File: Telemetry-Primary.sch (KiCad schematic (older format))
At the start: 34 parts

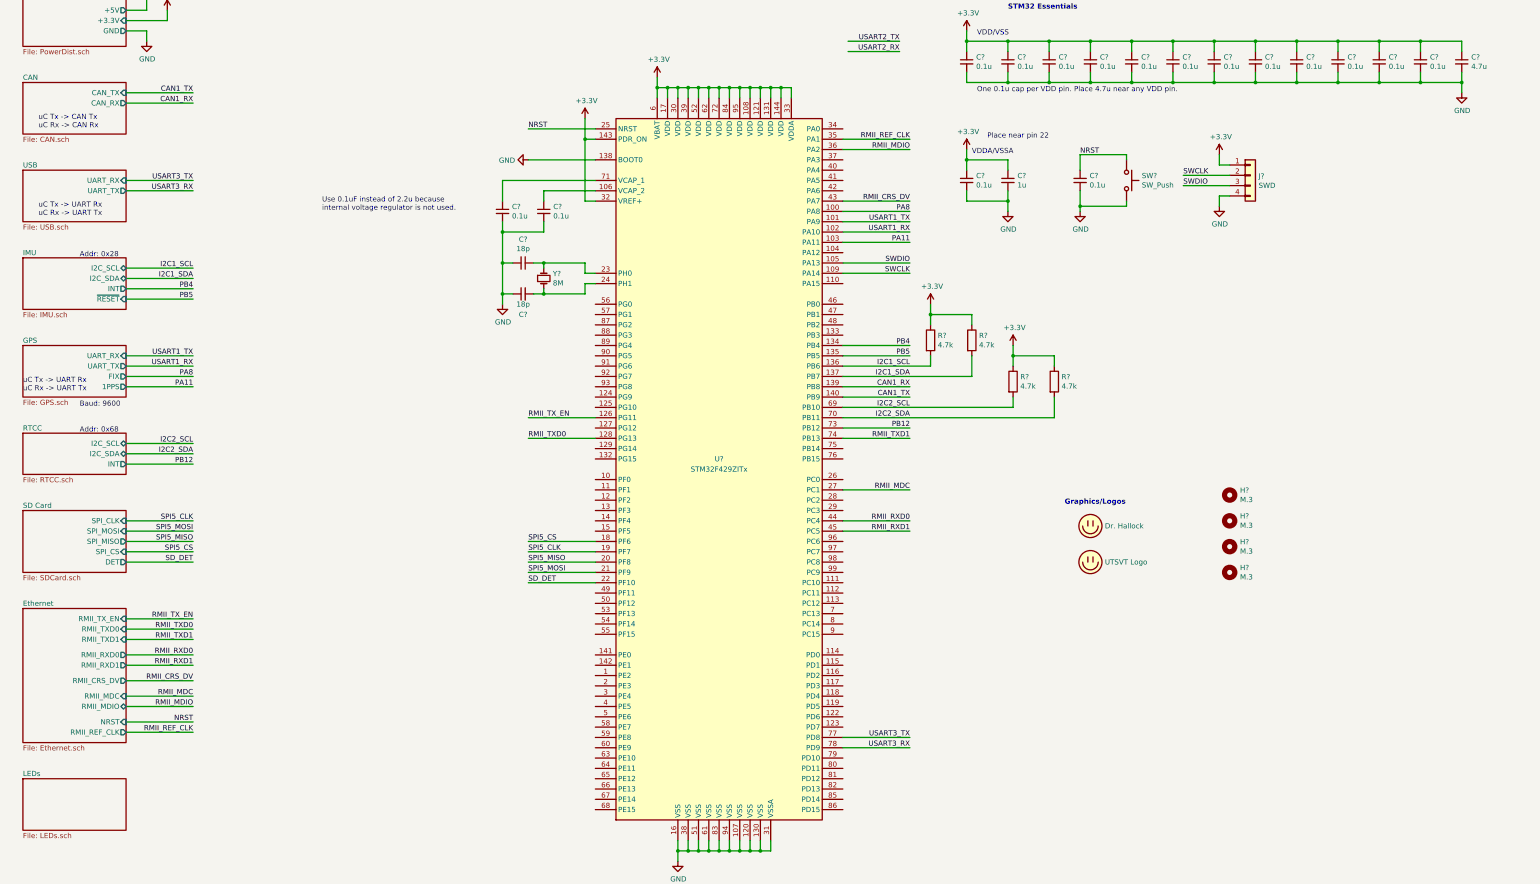
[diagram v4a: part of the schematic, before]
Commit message: Adds logic analyzer points and LEDs
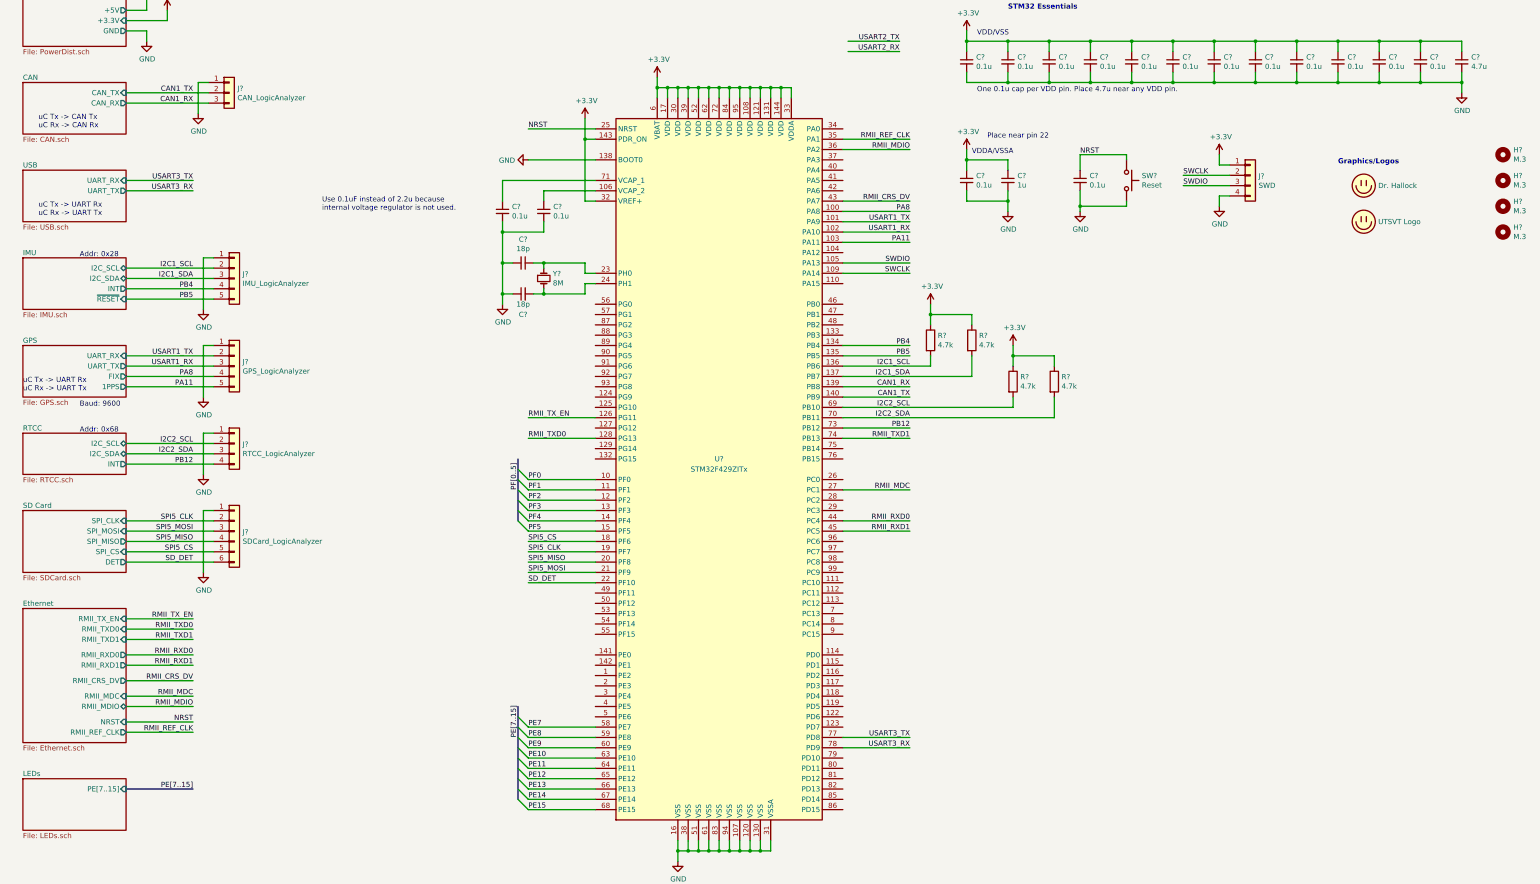
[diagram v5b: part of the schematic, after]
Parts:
- added J?: IMU_LogicAnalyzer, Connector_PinHeader_2.54mm:PinHeader_1x05_P2.54mm_Vertical, symbol Connector_Generic:Conn_01x05
- added J?: GPS_LogicAnalyzer, Connector_PinHeader_2.54mm:PinHeader_1x05_P2.54mm_Vertical, symbol Connector_Generic:Conn_01x05
- added J?: RTCC_LogicAnalyzer, Connector_PinHeader_2.54mm:PinHeader_1x04_P2.54mm_Vertical, symbol Connector_Generic:Conn_01x04
- added J?: SDCard_LogicAnalyzer, symbol Connector_Generic:Conn_01x06
- added J?: CAN_LogicAnalyzer, symbol Connector_Generic:Conn_01x03
- SW?: value SW_Push -> Reset; footprint (none) -> Button_Switch_SMD:SW_SPST_B3SL-1002P; P/N (none) -> EVQ-7Q203W or B3SL-1002P
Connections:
- net CAN1_RX: now also J?.3 (Pin_3)
- net CAN1_TX: now also J?.2 (Pin_2)
- net GND: now also J?.1 (Pin_1), J?.1 (Pin_1), J?.1 (Pin_1), J?.1 (Pin_1), J?.1 (Pin_1)
- net I2C1_SCL: now also J?.2 (Pin_2)
- net I2C1_SDA: now also J?.3 (Pin_3)
- net I2C2_SCL: now also J?.2 (Pin_2)
- net I2C2_SDA: now also J?.3 (Pin_3)
- net PA11: now also J?.5 (Pin_5)
- net PA8: now also J?.4 (Pin_4)
- net PB12: now also J?.4 (Pin_4)
- net PB4: now also J?.4 (Pin_4)
- net PB5: now also J?.5 (Pin_5)
- net SD_DET: now also J?.6 (Pin_6)
- net SPI5_CLK: now also J?.2 (Pin_2)
- net SPI5_CS: now also J?.5 (Pin_5)
- net SPI5_MISO: now also J?.4 (Pin_4)
- net SPI5_MOSI: now also J?.3 (Pin_3)
- net USART1_RX: now also J?.3 (Pin_3)
- net USART1_TX: now also J?.2 (Pin_2)
- net PF0: now reaches U?.10 (PF0)
- net PF1: now reaches U?.11 (PF1)
- net PF2: now reaches U?.12 (PF2)
- net PF3: now reaches U?.13 (PF3)
- net PF4: now reaches U?.14 (PF4)
- net PF5: now reaches U?.15 (PF5)
- net PE7: now reaches U?.58 (PE7)
- net PE8: now reaches U?.59 (PE8)
- net PE9: now reaches U?.60 (PE9)
- net PE10: now reaches U?.63 (PE10)
- net PE11: now reaches U?.64 (PE11)
- net PE12: now reaches U?.65 (PE12)
- net PE13: now reaches U?.66 (PE13)
- net PE14: now reaches U?.67 (PE14)
- net PE15: now reaches U?.68 (PE15)
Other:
- moved on the sheet: H?

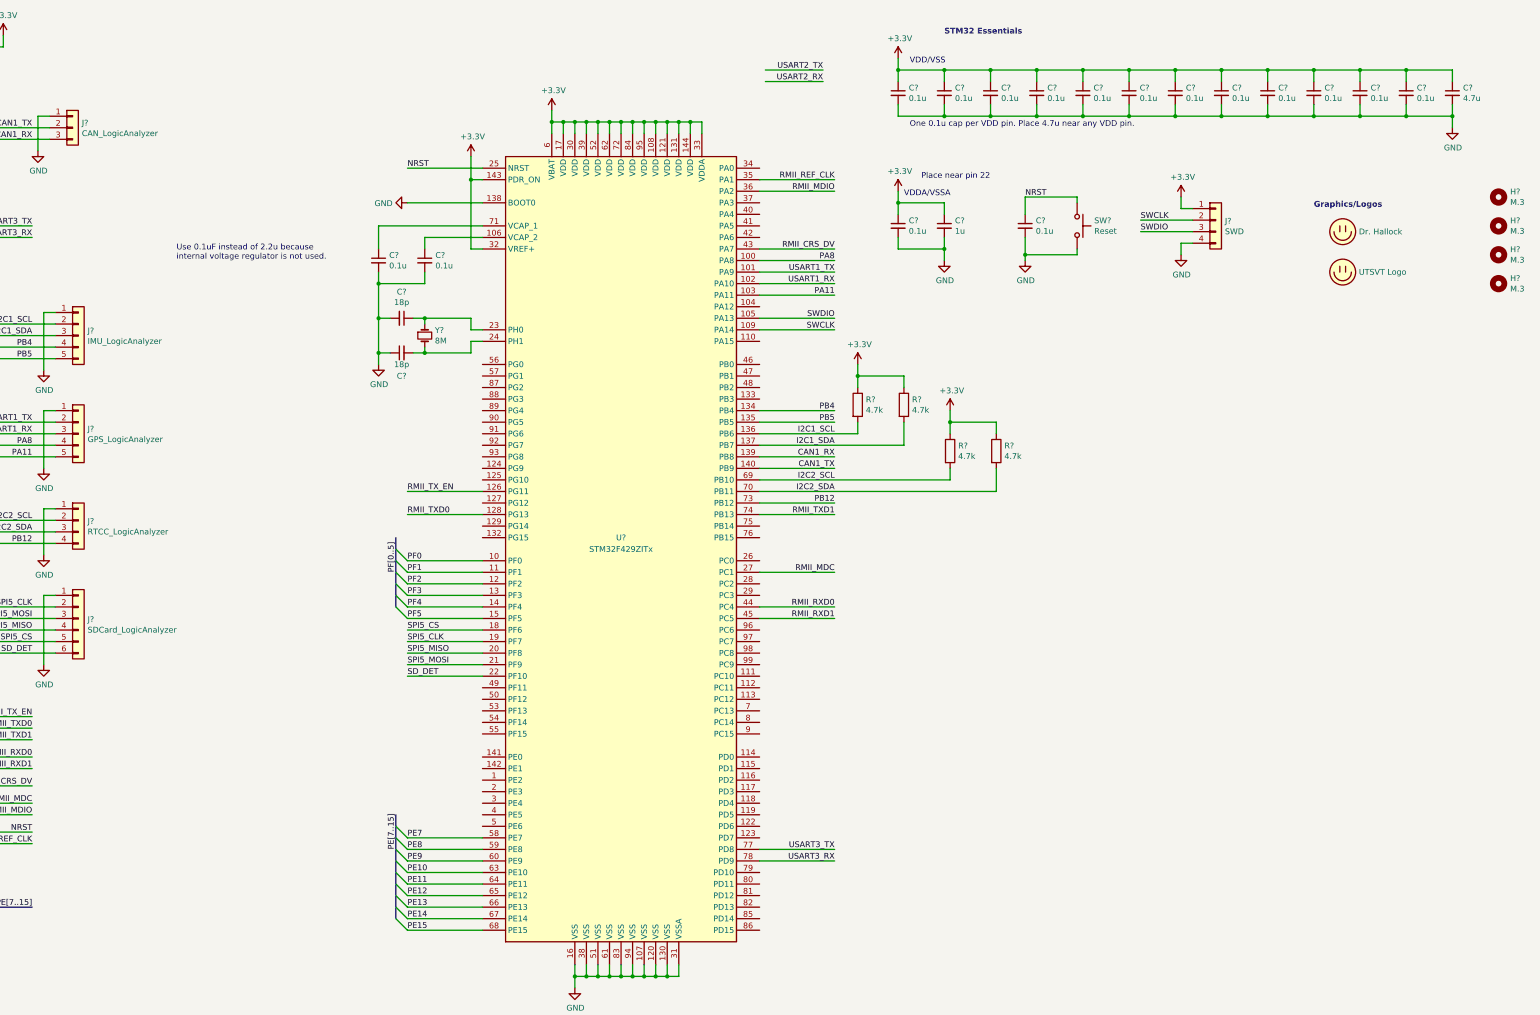
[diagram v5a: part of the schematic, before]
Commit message: Initial layout of the Telemtry board.
The ethernet interface needs more work.
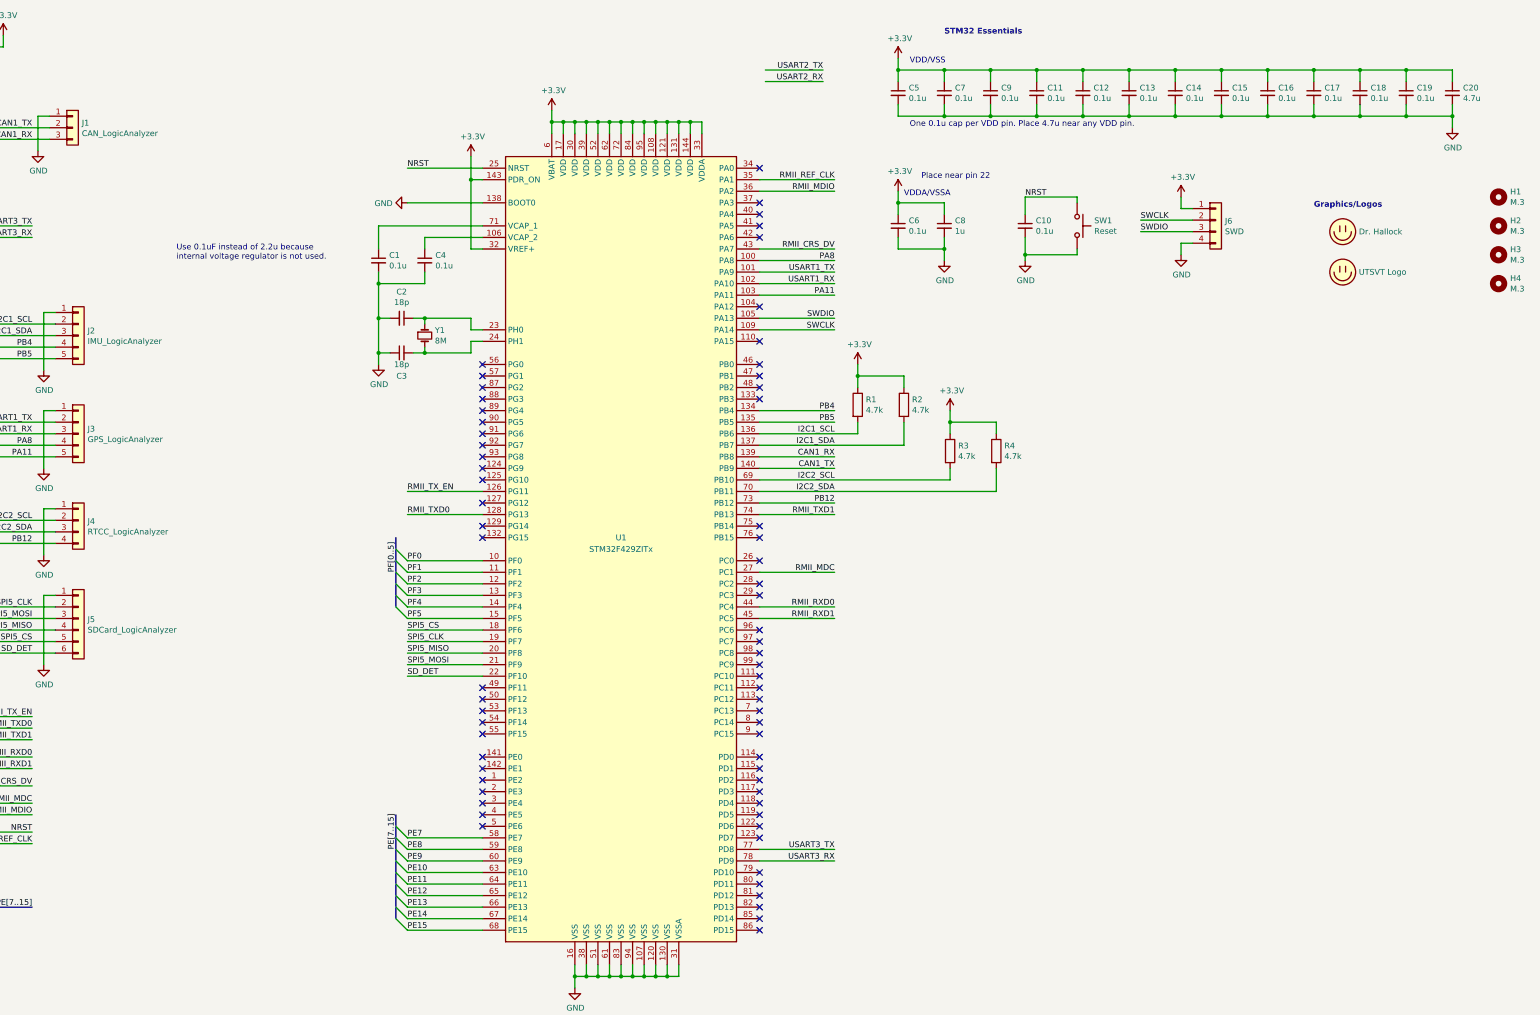
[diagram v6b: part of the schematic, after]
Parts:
- C1, C10, C11, C12, C13, C14, C15, C16, C17, C18, C19, C2, C20, C3, C4, C5, C6, C7, C8, C9: renamed from C?; footprint Capacitor_SMD:C_0805_2012Metri -> Capacitor_SMD:C_0805_2012Metric
- J1: renamed from J?; footprint (none) -> Connector_PinHeader_2.54mm:PinHeader_1x03_P2.54mm_Vertical
- J5: renamed from J?; footprint (none) -> Connector_PinHeader_2.54mm:PinHeader_1x06_P2.54mm_Vertical
- gave numbers to parts that had none: 17
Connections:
- no-connect marks 0 -> 66

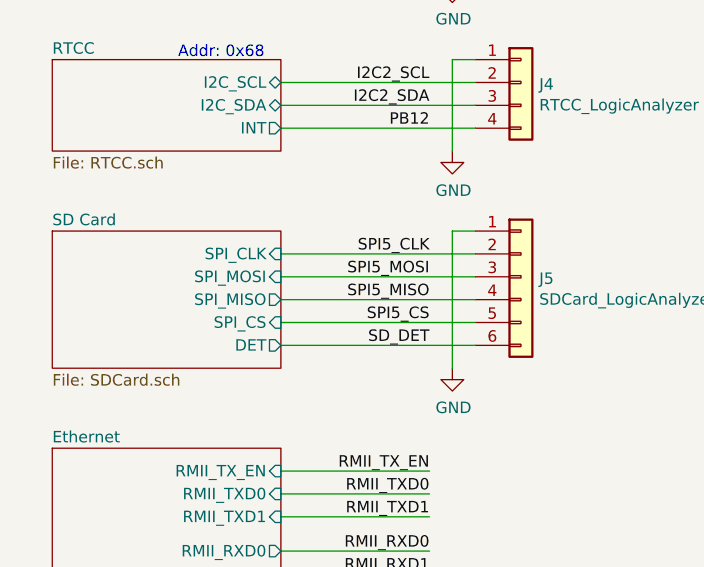
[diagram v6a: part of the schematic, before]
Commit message: Lay out the Telemetry board.
This is the initial draft of the Telemetry board layout. A few
debugging pins changed (on the SD card) for easier routing.

There is still some uncertainty with regard to the routing of the
Ethernet traces. According to my calculations, the differential
impedence between the RX+/- traces and the TX+/- traces is around
150R, which is 50% higher than one source was recommending. I am
uncertain how to reduce this though, and I am unclear as to how
much this will affect performance, especially when the traces
cover such a short distance.
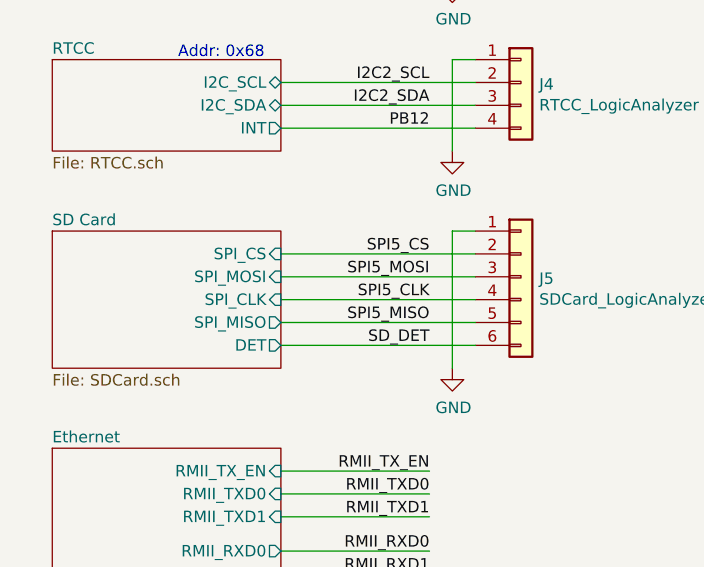
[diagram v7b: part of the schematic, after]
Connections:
- net SPI5_CLK: now also J5.4 (Pin_4); no longer J5.2 (Pin_2)
- net SPI5_CS: now also J5.2 (Pin_2); no longer J5.5 (Pin_5)
- net SPI5_MISO: now also J5.5 (Pin_5); no longer J5.4 (Pin_4)
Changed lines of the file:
@@
 F0 "SD Card" 50
 F1 "SDCard.sch" 50
-F2 "SPI_CS" I R 2000 6400 50
-F3 "SPI_MISO" O R 2000 6300 50
-F4 "SPI_CLK" I R 2000 6100 50
+F2 "SPI_CS" I R 2000 6100 50
+F3 "SPI_MISO" O R 2000 6400 50
+F4 "SPI_CLK" I R 2000 6300 50
 F5 "SPI_MOSI" I R 2000 6200 50
 F6 "DET" O R 2000 6500 50
@@
 Wire Wire Line
 	2000 6200 2850 6200
-Text Label 2650 6100 2    50   ~ 0
+Text Label 2650 6300 2    50   ~ 0
 SPI5_CLK
-Text Label 2650 6300 2    50   ~ 0
+Text Label 2650 6400 2    50   ~ 0
 SPI5_MISO
 Text Label 2650 6200 2    50   ~ 0
@@
 Wire Wire Line
 	2000 6400 2850 6400
-Text Label 2650 6400 2    50   ~ 0
+Text Label 2650 6100 2    50   ~ 0
 SPI5_CS
 Wire Wire Line
